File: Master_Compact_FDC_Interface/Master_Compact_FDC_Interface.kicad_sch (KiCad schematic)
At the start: 2 parts, among them J1 BBC, J2 Gotek

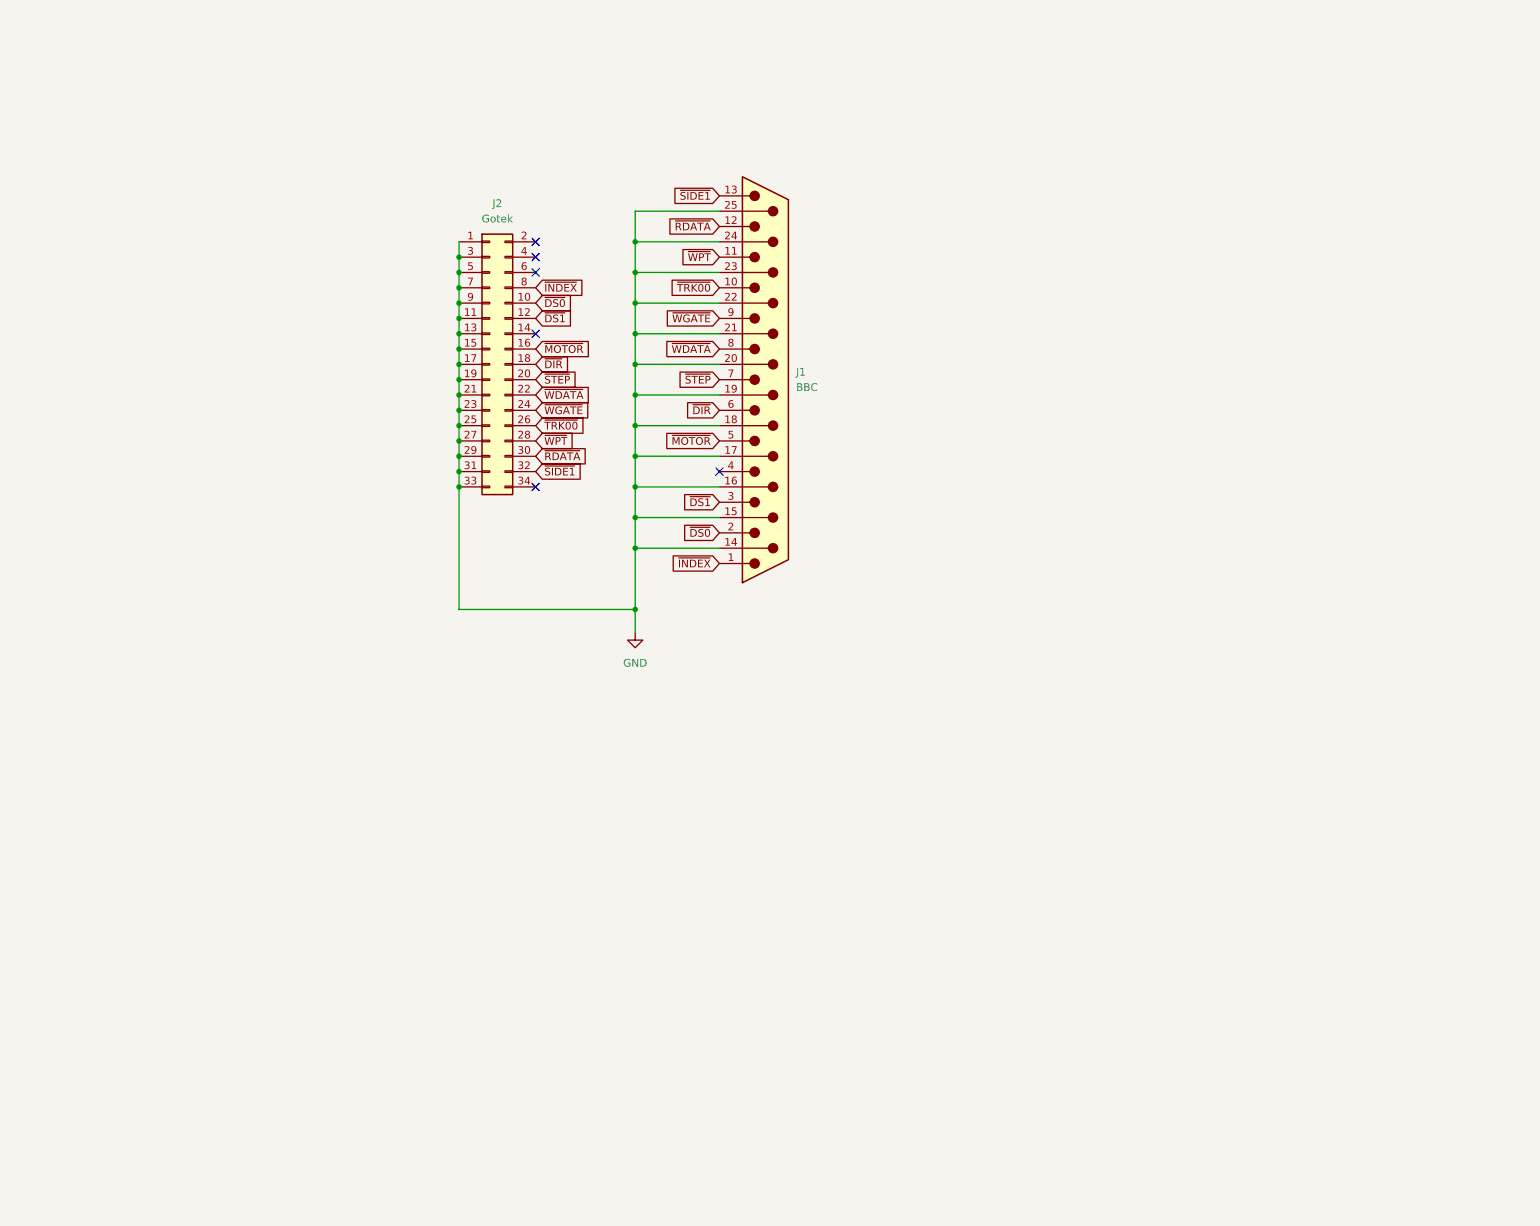
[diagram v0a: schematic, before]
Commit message: Reversed IDC header
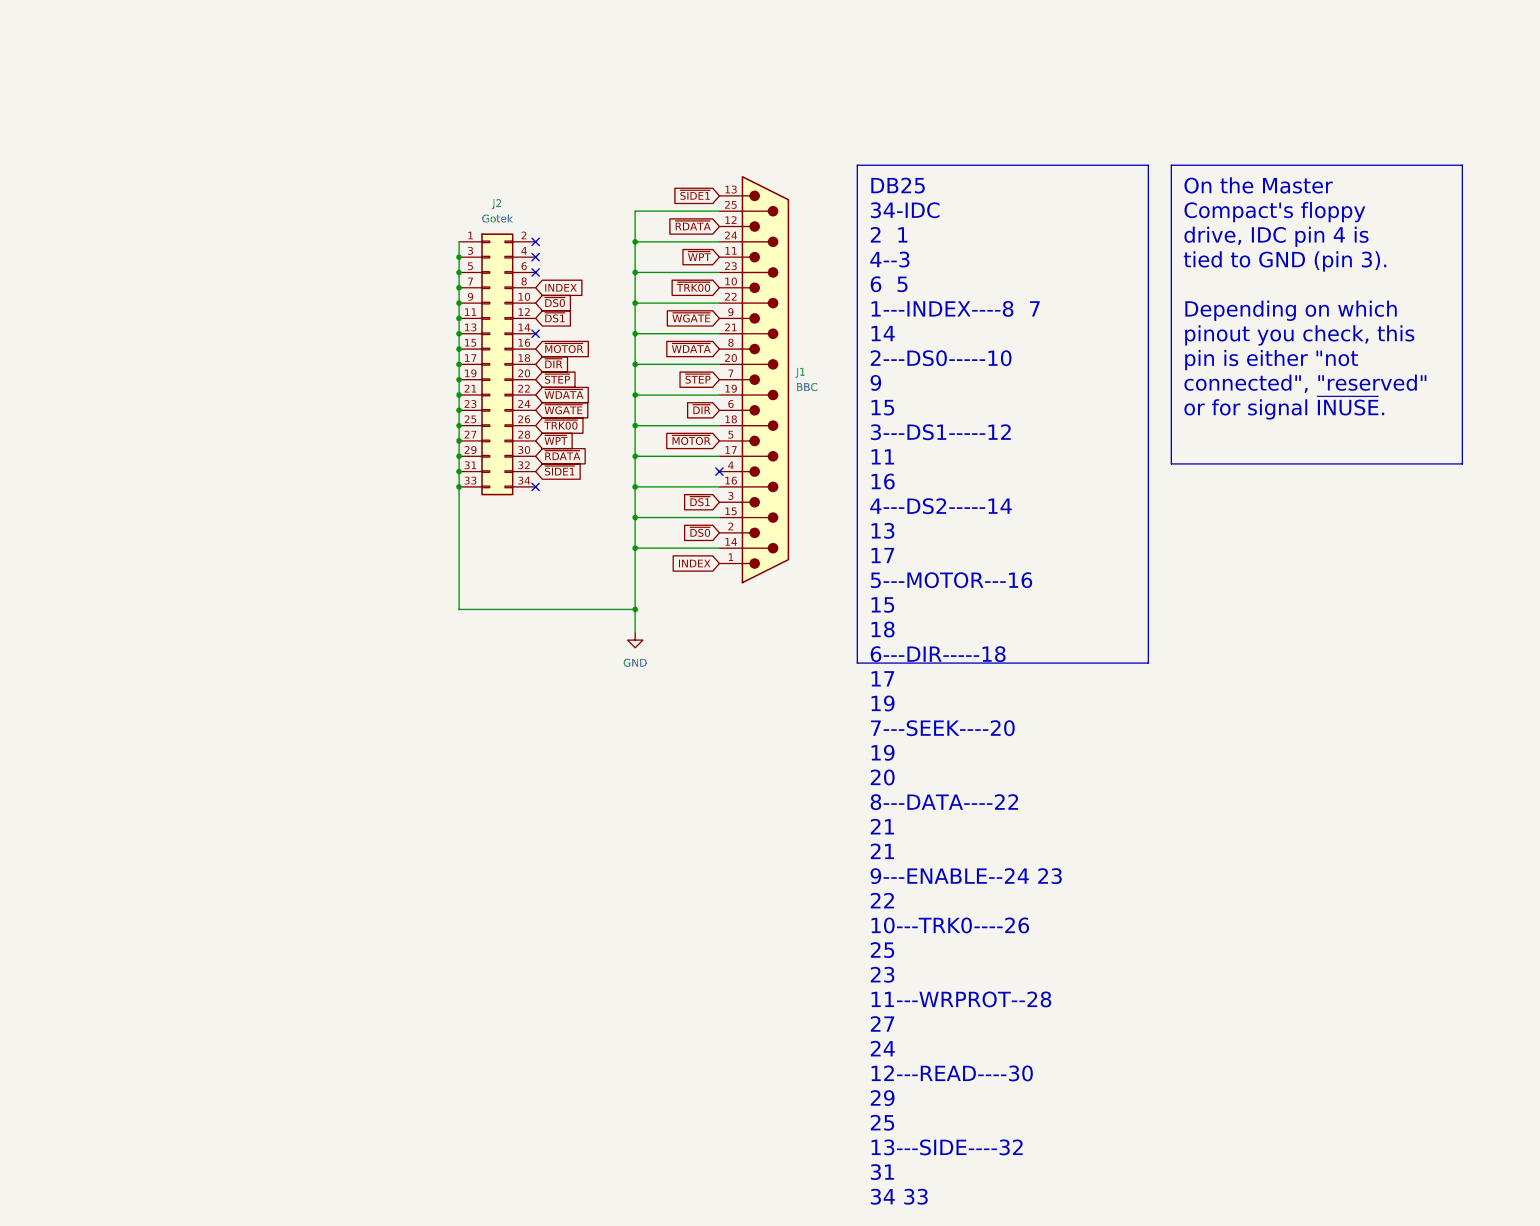
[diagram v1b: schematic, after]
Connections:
- net ~{INDEX} renamed INDEX
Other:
- company: (none) -> Brett Hallen
- title: (none) -> BBC Master Compact Floppy Adaptor
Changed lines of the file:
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@@
 (kicad_sch (version 20230121) (generator eeschema)
   (paper "A4")
+  (title_block
+    (title "BBC Master Compact Floppy Adaptor")
+    (date "17-Nov-2024")
+    (rev "1.1-0")
+    (company "Brett Hallen")
+    (comment 1 "WWW.YOUTUBE.COM/@BRFFF")
+  )
   (junction (at 125.73 104.14) (diameter 0) (color 0 0 0 0)
   )
@@
     (stroke (width 0) (type default))
   )
+  (text_box "On the Master Compact's floppy drive, IDC pin 4 is tied to GND (pin 3). \n\nDepending on which pinout you check, this pin is either \"not connected\", \"reserved\" or for signal ~{INUSE}."
+    (at 214.63 40.64 0) (size 48.26 49.53)
+    (stroke (width 0) (type default))
+    (fill (type none))
+    (effects (font (face "Consolas") (size 2.54 2.54)) (justify left top))
+  )
+  (text_box "DB25            34-IDC\n                 2  1\n                 4--3\n                 6  5\n    1---INDEX----8  7\n14  2---DS0-----10  9\n15  3---DS1-----12 11\n16  4---DS2-----14 13\n17  5---MOTOR---16 15\n18  6---DIR-----18 17\n19  7---SEEK----20 19\n20  8---DATA----22 21\n21  9---ENABLE--24 23\n22 10---TRK0----26 25\n23 11---WRPROT--28 27\n24 12---READ----30 29\n25 13---SIDE----32 31\n                34 33"
+    (at 162.56 40.64 0) (size 48.26 82.55)
+    (stroke (width 0) (type default))
+    (fill (type none))
+    (effects (font (face "Consolas") (size 2.54 2.54)) (justify left top))
+  )
   (global_label "~{MOTOR}" (shape input) (at 139.7 86.36 180) (fields_autoplaced)
     (effects (font (size 1.27 1.27)) (justify right))
@@
     )
   )
-  (global_label "~{INDEX}" (shape input) (at 109.22 60.96 0) (fields_autoplaced)
+  (global_label "INDEX" (shape input) (at 109.22 60.96 0) (fields_autoplaced)
     (effects (font (size 1.27 1.27)) (justify left))
     (property "Intersheetrefs" "${INTERSHEET_REFS}" (at 117.769 60.96 0)
@@
     )
   )
-  (global_label "~{INDEX}" (shape input) (at 139.7 106.68 180) (fields_autoplaced)
+  (global_label "INDEX" (shape input) (at 139.7 106.68 180) (fields_autoplaced)
     (effects (font (size 1.27 1.27)) (justify right))
     (property "Intersheetrefs" "${INTERSHEET_REFS}" (at 131.151 106.68 0)

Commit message: Added "schematic scraps" section
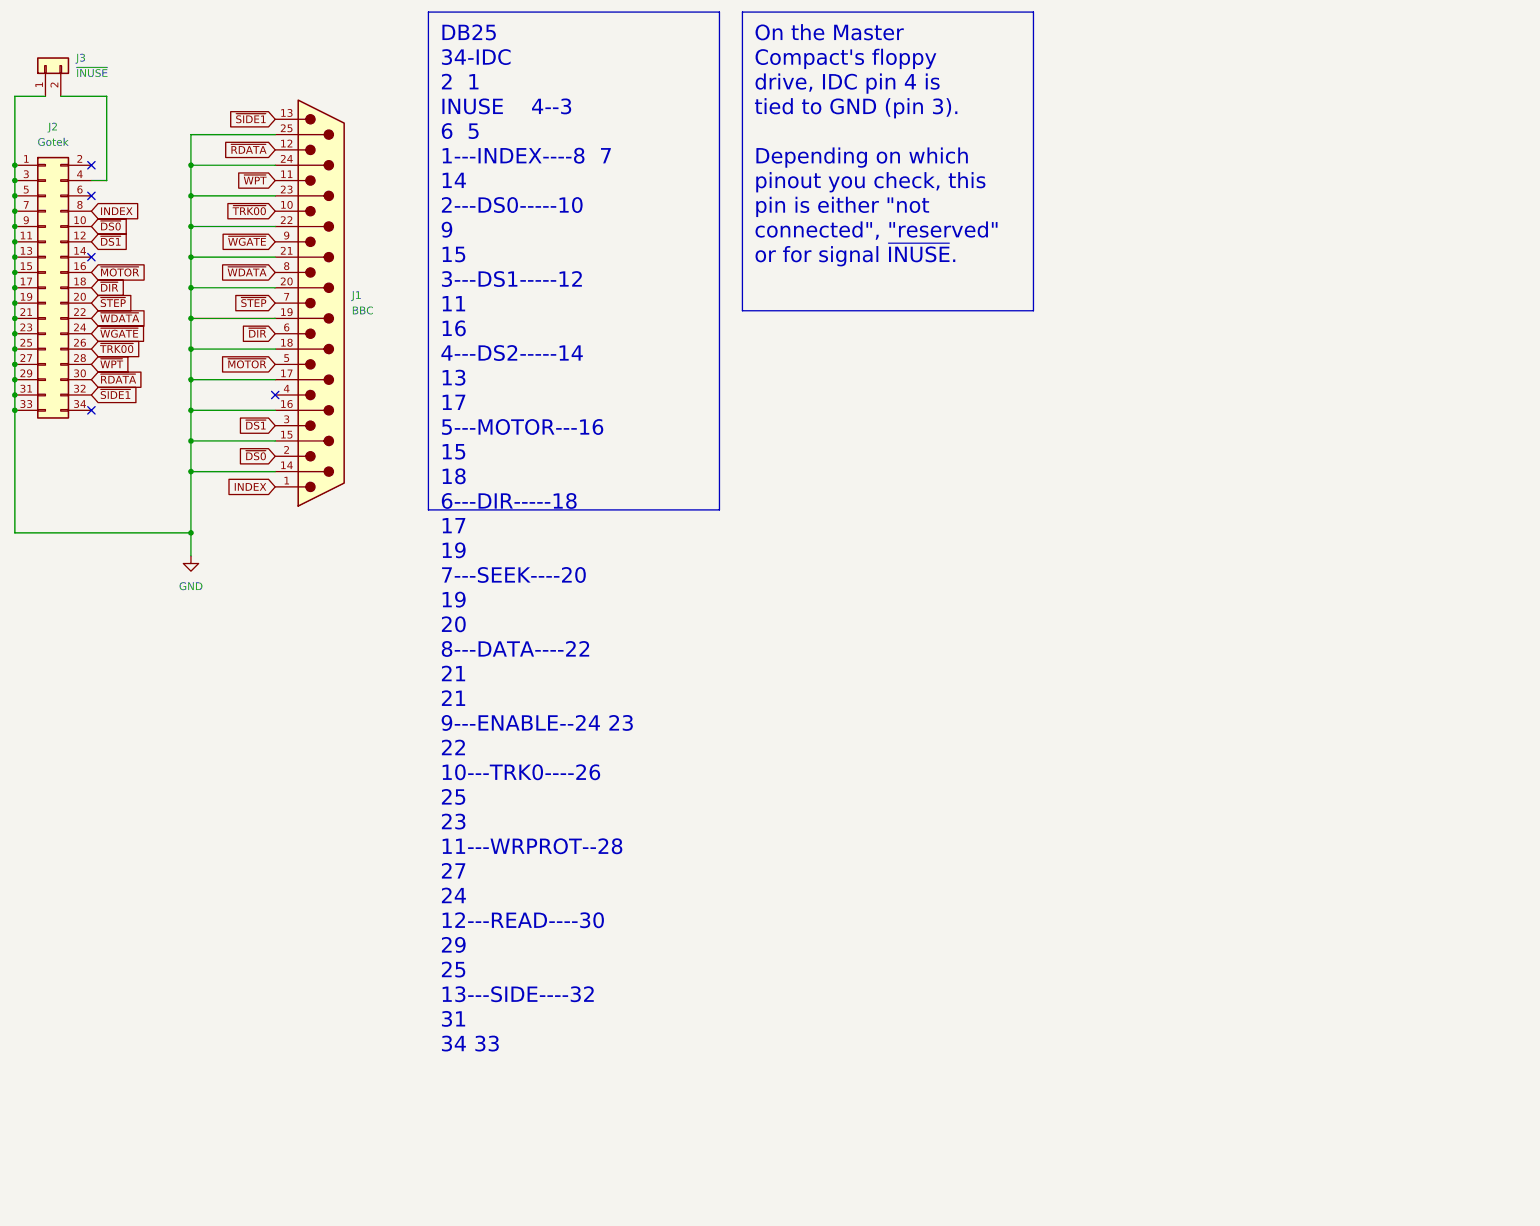
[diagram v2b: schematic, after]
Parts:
- added J3: ~{INUSE}, Connector_PinHeader_2.54mm:PinHeader_1x02_P2.54mm_Vertical, symbol Connector_Generic:Conn_01x02
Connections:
- net GND: now also J3.1 (Pin_1)
- net at J2.4 (Pin_4): now also J3.2 (Pin_2)
- no-connect marks 6 -> 5
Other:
- moved on the sheet: J1, J2
